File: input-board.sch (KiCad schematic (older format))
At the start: 70 parts, among them J1 BTNCON, J12 CAN, J2 BTNCON, J7 I2C, J8 GAS, J9 BREMSE, SW1 switch-with-led, SW2 switch-with-led, SW3 switch-with-led, SW4 switch-with-led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

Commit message: start of layout
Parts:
- D1, D2, D3, D4, D5, D6, D7, D8: symbol boardcomputer:CDSOD323 -> input-board-rescue:CDSOD323-boardcomputer
- J2: footprint Connector_Molex:Molex_PicoBlade_53047-0410_1x04_P1.25mm_Vertical -> Connector_Molex:Molex_PicoBlade_53048-0410_1x04_P1.25mm_Horizontal
- SW1, SW2, SW3, SW4: footprint input-board:switch-19mm -> input-board:switch-16mm
- U1: symbol boardcomputer:MPM3620 -> input-board-rescue:MPM3620-boardcomputer
- gave numbers to parts that had none: 9
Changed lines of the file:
@@
 	6650 5700 6450 5700
 $Comp
-L boardcomputer:MPM3620 U1
+L input-board-rescue:MPM3620-boardcomputer U1
 U 1 1 601CF94B
 P 8950 1450
@@
 	5300 4950 5300 4850
 $Comp
-L boardcomputer:CDSOD323 D1
+L input-board-rescue:CDSOD323-boardcomputer D1
 U 1 1 60339500
 P 8150 5800
@@
 F 0 "SW4" H 1200 4021 50  0000 C CNN
 F 1 "switch-with-led" H 1200 3930 50  0000 C CNN
-F 2 "input-board:switch-19mm" H 1150 3650 50  0001 C CNN
+F 2 "input-board:switch-16mm" H 1150 3650 50  0001 C CNN
 F 3 "" H 1150 3650 50  0001 C CNN
 	1    1200 3650
@@
 F 0 "SW3" H 1200 3121 50  0000 C CNN
 F 1 "switch-with-led" H 1200 3030 50  0000 C CNN
-F 2 "input-board:switch-19mm" H 1150 2750 50  0001 C CNN
+F 2 "input-board:switch-16mm" H 1150 2750 50  0001 C CNN
 F 3 "" H 1150 2750 50  0001 C CNN
 	1    1200 2750
@@
 F 0 "SW2" H 1200 2271 50  0000 C CNN
 F 1 "switch-with-led" H 1200 2180 50  0000 C CNN
-F 2 "input-board:switch-19mm" H 1150 1900 50  0001 C CNN
+F 2 "input-board:switch-16mm" H 1150 1900 50  0001 C CNN
 F 3 "" H 1150 1900 50  0001 C CNN
 	1    1200 1900
@@
 F 0 "SW1" H 1200 1421 50  0000 C CNN
 F 1 "switch-with-led" H 1200 1330 50  0000 C CNN
-F 2 "input-board:switch-19mm" H 1150 1050 50  0001 C CNN
+F 2 "input-board:switch-16mm" H 1150 1050 50  0001 C CNN
 F 3 "" H 1150 1050 50  0001 C CNN
 	1    1200 1050
@@
 	9250 6000 9550 6000
 $Comp
-L boardcomputer:CDSOD323 D2
+L input-board-rescue:CDSOD323-boardcomputer D2
 U 1 1 603375D7
 P 9850 5800
@@
 	3250 2600 3550 2600
 $Comp
-L boardcomputer:CDSOD323 D4
+L input-board-rescue:CDSOD323-boardcomputer D4
 U 1 1 6033E4AF
 P 3550 2400
@@
 	3250 3300 3550 3300
 $Comp
-L boardcomputer:CDSOD323 D5
-U 1 1 603B76B7
-P 3550 3100
-F 0 "D5" V 3554 3230 50  0000 L CNN
-F 1 "CDSOD323" V 3645 3230 50  0000 L CNN
-F 2 "Diode_SMD:D_SOD-323" H 3550 3250 50  0001 C CNN
-F 3 "" H 3550 3250 50  0001 C CNN
-	1    3550 3100
-	0    1    1    0
-$EndComp
-$Comp
 L Device:C C7
 U 1 1 603B76BD
@@
 	3250 1900 3550 1900
 $Comp
-L boardcomputer:CDSOD323 D3
+L input-board-rescue:CDSOD323-boardcomputer D3
 U 1 1 603C8813
 P 3550 1700
@@
 F 0 "J2" V 2114 4212 50  0000 R CNN
 F 1 "BTNCON" V 2250 4650 50  0000 R CNN
-F 2 "Connector_Molex:Molex_PicoBlade_53047-0410_1x04_P1.25mm_Vertical" H 2150 4500 50  0001 C CNN
+F 2 "Connector_Molex:Molex_PicoBlade_53048-0410_1x04_P1.25mm_Horizontal" H 2150 4500 50  0001 C CNN
 F 3 "~" H 2150 4500 50  0001 C CNN
 	1    2150 4500
@@
 	3250 4700 3550 4700
 $Comp
-L boardcomputer:CDSOD323 D7
+L input-board-rescue:CDSOD323-boardcomputer D7
 U 1 1 60404627
 P 3550 4500
@@
 	3250 5400 3550 5400
 $Comp
-L boardcomputer:CDSOD323 D8
+L input-board-rescue:CDSOD323-boardcomputer D8
 U 1 1 60404651
 P 3550 5200
@@
 	3250 4000 3550 4000
 $Comp
-L boardcomputer:CDSOD323 D6
+L input-board-rescue:CDSOD323-boardcomputer D6
 U 1 1 6040467B
 P 3550 3800
@@
 MDLED4
 $Comp
-L Connector_Generic:Conn_01x04 J?
+L Connector_Generic:Conn_01x04 J3
 U 1 1 604193E6
 P 7100 4750
-F 0 "J?" V 7064 4462 50  0000 R CNN
+F 0 "J3" V 7064 4462 50  0000 R CNN
 F 1 "SWD" V 7200 4900 50  0000 R CNN
 F 2 "Connector_PinHeader_2.54mm:PinHeader_1x04_P2.54mm_Vertical" H 7100 4750 50  0001 C CNN
@@
 SWDIO
 $Comp
-L power:GND #PWR?
+L power:GND #PWR0105
 U 1 1 604368D8
 P 7300 4850
-F 0 "#PWR?" H 7300 4600 50  0001 C CNN
+F 0 "#PWR0105" H 7300 4600 50  0001 C CNN
 F 1 "GND" V 7305 4722 50  0000 R CNN
 F 2 "" H 7300 4850 50  0001 C CNN
@@
 $EndComp
 $Comp
-L power:+3V3 #PWR?
+L power:+3V3 #PWR0106
 U 1 1 60436CB5
 P 7300 4550
-F 0 "#PWR?" H 7300 4400 50  0001 C CNN
+F 0 "#PWR0106" H 7300 4400 50  0001 C CNN
 F 1 "+3V3" H 7315 4723 50  0000 C CNN
 F 2 "" H 7300 4550 50  0001 C CNN
@@
 $EndComp
 $Comp
-L Device:R R?
+L Device:R R24
 U 1 1 604431E6
 P 4750 950
-F 0 "R?" V 4850 950 50  0000 L CNN
+F 0 "R24" V 4850 950 50  0000 L CNN
 F 1 "10k" V 4850 800 50  0000 L CNN
 F 2 "Resistor_SMD:R_0603_1608Metric" V 4680 950 50  0001 C CNN
@@
 $EndComp
 $Comp
-L power:+3V3 #PWR?
+L power:+3V3 #PWR0107
 U 1 1 604431EC
 P 4750 800
-F 0 "#PWR?" H 4750 650 50  0001 C CNN
+F 0 "#PWR0107" H 4750 650 50  0001 C CNN
 F 1 "+3V3" H 4765 973 50  0000 C CNN
 F 2 "" H 4750 800 50  0001 C CNN
@@
 	4750 1100 5000 1100
 $Comp
-L Device:R R?
+L Device:R R25
 U 1 1 6045D388
 P 4750 2400
-F 0 "R?" V 4850 2450 50  0000 L CNN
+F 0 "R25" V 4850 2450 50  0000 L CNN
 F 1 "100k" V 4850 2250 50  0000 L CNN
 F 2 "Resistor_SMD:R_0603_1608Metric" V 4680 2400 50  0001 C CNN
@@
 $EndComp
 $Comp
-L power:GND #PWR?
+L power:GND #PWR0108
 U 1 1 6045DA92
 P 4500 2400
-F 0 "#PWR?" H 4500 2150 50  0001 C CNN
+F 0 "#PWR0108" H 4500 2150 50  0001 C CNN
 F 1 "GND" V 4505 2272 50  0000 R CNN
 F 2 "" H 4500 2400 50  0001 C CNN
@@
 	4600 2400 4500 2400
 $Comp
-L Device:R R?
+L Device:R R23
 U 1 1 6047099B
 P 4500 950
-F 0 "R?" V 4600 950 50  0000 L CNN
+F 0 "R23" V 4600 950 50  0000 L CNN
 F 1 "10k" V 4600 800 50  0000 L CNN
 F 2 "Resistor_SMD:R_0603_1608Metric" V 4430 950 50  0001 C CNN
@@
 $EndComp
 $Comp
-L Device:R R?
+L Device:R R22
 U 1 1 6047A8E0
 P 4300 1300
-F 0 "R?" V 4400 1300 50  0000 L CNN
+F 0 "R22" V 4400 1300 50  0000 L CNN
 F 1 "10k" V 4400 1150 50  0000 L CNN
 F 2 "Resistor_SMD:R_0603_1608Metric" V 4230 1300 50  0001 C CNN
@@
 $EndComp
 $Comp
-L power:GND #PWR?
+L power:GND #PWR0109
 U 1 1 6047AFB7
 P 4100 1350
-F 0 "#PWR?" H 4100 1100 50  0001 C CNN
+F 0 "#PWR0109" H 4100 1100 50  0001 C CNN
 F 1 "GND" V 4105 1222 50  0000 R CNN
 F 2 "" H 4100 1350 50  0001 C CNN
@@
 	4500 1300 5000 1300
 $Comp
-L power:+3V3 #PWR?
+L power:+3V3 #PWR0110
 U 1 1 604A0FE2
 P 4500 800
-F 0 "#PWR?" H 4500 650 50  0001 C CNN
+F 0 "#PWR0110" H 4500 650 50  0001 C CNN
 F 1 "+3V3" H 4515 973 50  0000 C CNN
 F 2 "" H 4500 800 50  0001 C CNN
@@
 RAW_BREMSE
 $Comp
-L Device:C C?
+L Device:C C13
 U 1 1 604A5B63
 P 6550 1450
-F 0 "C?" H 6650 1550 50  0000 C CNN
+F 0 "C13" H 6650 1550 50  0000 C CNN
 F 1 "100n" H 6450 1550 50  0000 C CNN
 F 2 "Capacitor_SMD:C_0603_1608Metric" H 6588 1300 50  0001 C CNN
@@
 $EndComp
 $Comp
-L power:+3V3 #PWR?
+L power:+3V3 #PWR0111
 U 1 1 604A70A4
 P 6550 1300
-F 0 "#PWR?" H 6550 1150 50  0001 C CNN
+F 0 "#PWR0111" H 6550 1150 50  0001 C CNN
 F 1 "+3V3" H 6565 1473 50  0000 C CNN
 F 2 "" H 6550 1300 50  0001 C CNN
@@
 $EndComp
 $Comp
-L power:GND #PWR?
+L power:GND #PWR0112
 U 1 1 604A7536
 P 6550 1600
-F 0 "#PWR?" H 6550 1350 50  0001 C CNN
+F 0 "#PWR0112" H 6550 1350 50  0001 C CNN
 F 1 "GND" V 6555 1472 50  0000 R CNN
 F 2 "" H 6550 1600 50  0001 C CNN
@@
 $EndComp
 $Comp
-L Device:C C?
+L Device:C C14
 U 1 1 604B1696
 P 6900 1450
-F 0 "C?" H 7000 1550 50  0000 C CNN
+F 0 "C14" H 7000 1550 50  0000 C CNN
 F 1 "100n" H 6800 1550 50  0000 C CNN
 F 2 "Capacitor_SMD:C_0603_1608Metric" H 6938 1300 50  0001 C CNN
@@
 $EndComp
 $Comp
-L power:+3V3 #PWR?
+L power:+3V3 #PWR0113
 U 1 1 604B169C
 P 6900 1300
-F 0 "#PWR?" H 6900 1150 50  0001 C CNN
+F 0 "#PWR0113" H 6900 1150 50  0001 C CNN
 F 1 "+3V3" H 6915 1473 50  0000 C CNN
 F 2 "" H 6900 1300 50  0001 C CNN
@@
 $EndComp
 $Comp
-L power:GND #PWR?
+L power:GND #PWR0114
 U 1 1 604B16A2
 P 6900 1600
-F 0 "#PWR?" H 6900 1350 50  0001 C CNN
+F 0 "#PWR0114" H 6900 1350 50  0001 C CNN
 F 1 "GND" V 6905 1472 50  0000 R CNN
 F 2 "" H 6900 1600 50  0001 C CNN
@@
 $EndComp
 $Comp
-L Device:C C?
+L Device:C C15
 U 1 1 604BAED3
 P 7250 1450
-F 0 "C?" H 7350 1550 50  0000 C CNN
+F 0 "C15" H 7350 1550 50  0000 C CNN
 F 1 "100n" H 7150 1550 50  0000 C CNN
 F 2 "Capacitor_SMD:C_0603_1608Metric" H 7288 1300 50  0001 C CNN
@@
 $EndComp
 $Comp
-L power:+3V3 #PWR?
+L power:+3V3 #PWR0115
 U 1 1 604BAED9
 P 7250 1300
-F 0 "#PWR?" H 7250 1150 50  0001 C CNN
+F 0 "#PWR0115" H 7250 1150 50  0001 C CNN
 F 1 "+3V3" H 7265 1473 50  0000 C CNN
 F 2 "" H 7250 1300 50  0001 C CNN
@@
 $EndComp
 $Comp
-L power:GND #PWR?
+L power:GND #PWR0116
 U 1 1 604BAEDF
 P 7250 1600
-F 0 "#PWR?" H 7250 1350 50  0001 C CNN
+F 0 "#PWR0116" H 7250 1350 50  0001 C CNN
 F 1 "GND" V 7255 1472 50  0000 R CNN
 F 2 "" H 7250 1600 50  0001 C CNN
@@
 $EndComp
 $Comp
-L Device:C C?
+L Device:C C16
 U 1 1 604C50A6
 P 7250 2300
-F 0 "C?" H 7350 2400 50  0000 C CNN
+F 0 "C16" H 7350 2400 50  0000 C CNN
 F 1 "100n" H 7150 2400 50  0000 C CNN
 F 2 "Capacitor_SMD:C_0603_1608Metric" H 7288 2150 50  0001 C CNN
@@
 $EndComp
 $Comp
-L power:+3V3 #PWR?
+L power:+3V3 #PWR0117
 U 1 1 604C50AC
 P 7250 2150
-F 0 "#PWR?" H 7250 2000 50  0001 C CNN
+F 0 "#PWR0117" H 7250 2000 50  0001 C CNN
 F 1 "+3V3" H 7265 2323 50  0000 C CNN
 F 2 "" H 7250 2150 50  0001 C CNN
@@
 $EndComp
 $Comp
-L power:GND #PWR?
+L power:GND #PWR0122
 U 1 1 604C50B2
 P 7250 2450
-F 0 "#PWR?" H 7250 2200 50  0001 C CNN
+F 0 "#PWR0122" H 7250 2200 50  0001 C CNN
 F 1 "GND" V 7255 2322 50  0000 R CNN
 F 2 "" H 7250 2450 50  0001 C CNN
@@
 	1    0    0    -1
 $EndComp
+$Comp
+L input-board-rescue:CDSOD323-boardcomputer D5
+U 1 1 603B76B7
+P 3550 3100
+F 0 "D5" V 3554 3230 50  0000 L CNN
+F 1 "CDSOD323" V 3645 3230 50  0000 L CNN
+F 2 "Diode_SMD:D_SOD-323" H 3550 3250 50  0001 C CNN
+F 3 "" H 3550 3250 50  0001 C CNN
+	1    3550 3100
+	0    1    1    0
+$EndComp
 $EndSCHEMATC

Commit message: more layouting
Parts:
- added C17: 100n, Capacitor_SMD:C_0603_1608Metric, symbol Device:C
- added X1: ASCO, Oscillator:Oscillator_SMD_Abracon_ASDMB-4Pin_2.5x2.0mm, symbol Oscillator:ASDMB-xxxMHz
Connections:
- net +3V3: now also C17.2, X1.1 (Standby), X1.4 (VDD)
- net BTN1: now also U2.40 (PB4); no longer U2.39 (PB3)
- net BTN2: now also U2.39 (PB3); no longer U2.40 (PB4)
- net BTN3: now also U2.38 (PA15); no longer U2.31 (PA10)
- net BTN4: now also U2.25 (PB12); no longer U2.42 (PB6)
- net BTN5: now also U2.22 (PB11); no longer U2.43 (PB7)
- net BTN6: now also U2.21 (PB10); no longer U2.38 (PA15)
- net GND: now also SW1.2, SW2.2, C17.1, X1.2 (GND); no longer SW1.1, SW2.1
- net MDBT1: now also SW1.1, U2.43 (PB7); no longer SW1.2, U2.18 (PB0)
- net MDBT2: now also SW2.1, U2.29 (PA8); no longer SW2.2, U2.21 (PB10)
- net MDBT3: now also U2.26 (PB13); no longer U2.25 (PB12)
- net MDBT4: now also U2.18 (PB0); no longer U2.27 (PB14)
- net MDLED1: now also U2.42 (PB6); no longer U2.19 (PB1)
- net MDLED2: now also U2.28 (PB15); no longer U2.22 (PB11)
- net MDLED3: now also U2.27 (PB14); no longer U2.26 (PB13)
- net MDLED4: now also U2.19 (PB1); no longer U2.28 (PB15)
- net at U2.5 (PD0): now also X1.3 (Out)
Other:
- note added: "3V3"
- note added: "5V"
- moved on the sheet: C5, C6, C7, D3, D4, D5, J1, R11, R17, R18, R5, R6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

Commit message: Added input reverse protection
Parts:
- added D9: D_Schottky, Diode_SMD:D_SOD-123, symbol Device:D_Schottky
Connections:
- net 15V: now also D9.1 (K); no longer J12.1 (Pin_1)
- new net: D9.2 (A), J12.1 (Pin_1)
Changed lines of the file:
@@
 Text GLabel 6650 5400 2    50   Input ~ 0
 GND
-Text GLabel 6650 5700 2    50   Input ~ 0
+Text GLabel 6750 5700 2    50   Input ~ 0
 15V
 Text GLabel 6650 5600 2    50   Input ~ 0
@@
 Wire Wire Line
 	6450 5600 6650 5600
-Wire Wire Line
-	6650 5700 6450 5700
 $Comp
 L input-board-rescue:MPM3620-boardcomputer U1
@@
 3V3
 $Comp
-L power:GND #PWR?
+L power:GND #PWR027
 U 1 1 6045ABEF
 P 1400 4200
-F 0 "#PWR?" H 1400 3950 50  0001 C CNN
+F 0 "#PWR027" H 1400 3950 50  0001 C CNN
 F 1 "GND" V 1405 4027 50  0000 C CNN
 F 2 "" H 1400 4200 50  0001 C CNN
@@
 $EndComp
 $Comp
-L power:GND #PWR?
+L power:GND #PWR028
 U 1 1 6045B33D
 P 1400 5050
-F 0 "#PWR?" H 1400 4800 50  0001 C CNN
+F 0 "#PWR028" H 1400 4800 50  0001 C CNN
 F 1 "GND" V 1405 4877 50  0000 C CNN
 F 2 "" H 1400 5050 50  0001 C CNN
@@
 	0    -1   -1   0
 $EndComp
+$Comp
+L Device:D_Schottky D9
+U 1 1 603427AF
+P 6600 5700
+F 0 "D9" H 6750 5800 50  0000 C CNN
+F 1 "D_Schottky" H 6450 5800 50  0000 C CNN
+F 2 "Diode_SMD:D_SOD-123" H 6600 5700 50  0001 C CNN
+F 3 "~" H 6600 5700 50  0001 C CNN
+	1    6600 5700
+	-1   0    0    1
+$EndComp
 $EndSCHEMATC

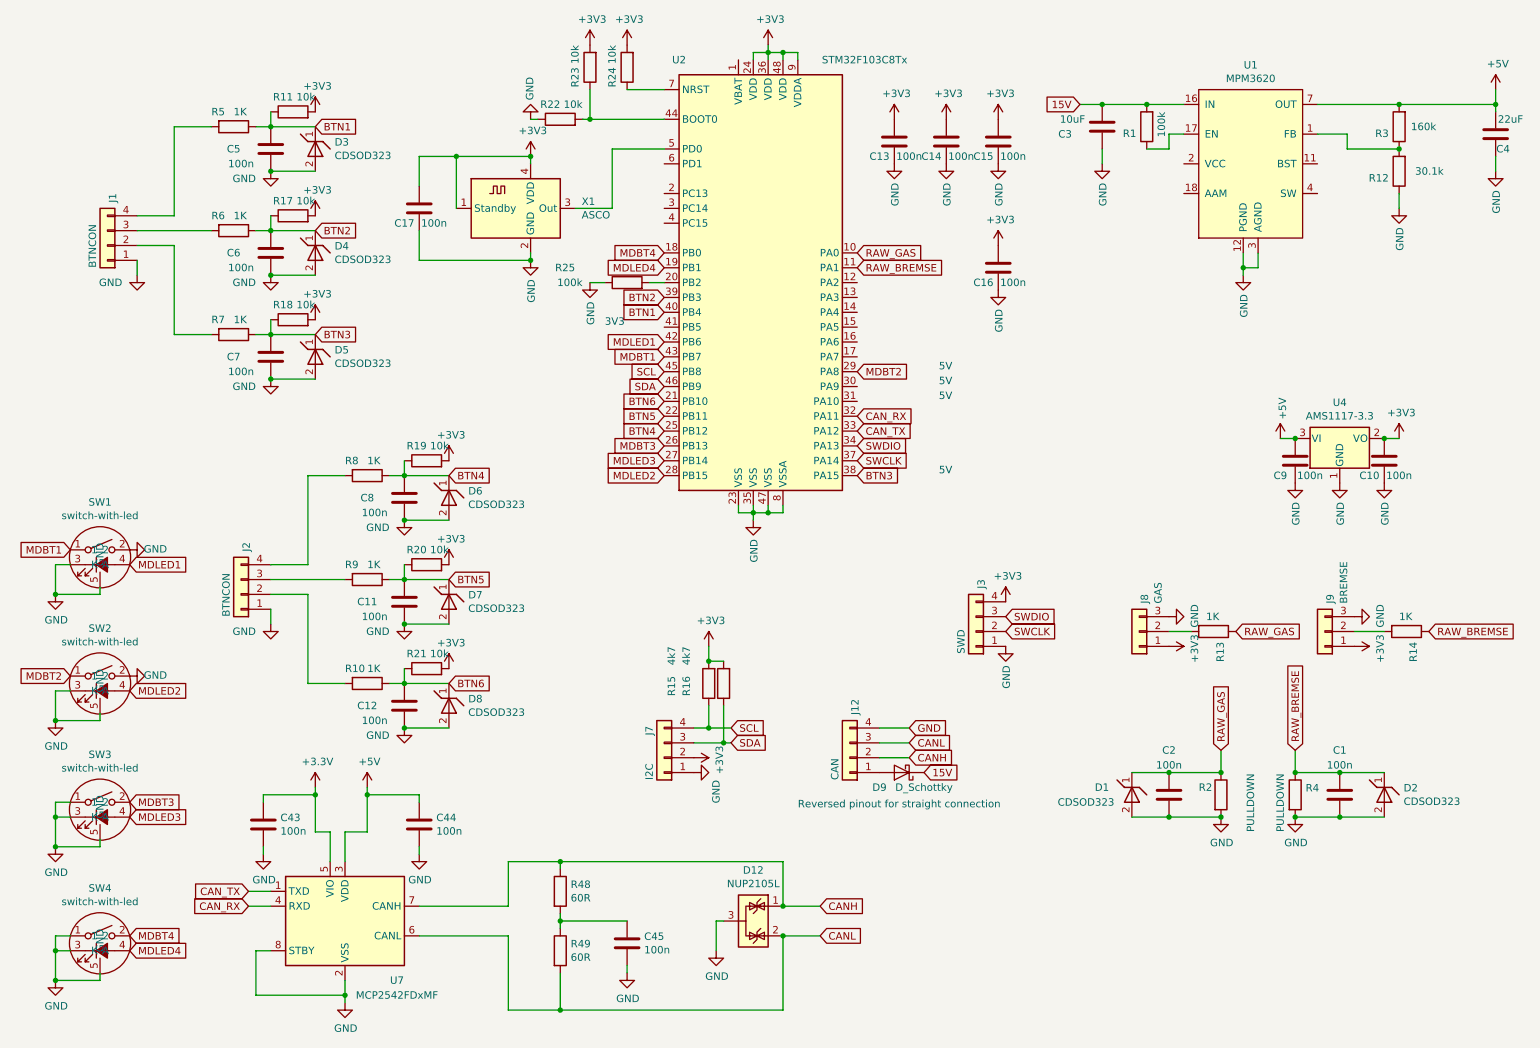
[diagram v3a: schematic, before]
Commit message: Changed input to LDO Added JLCPCB #
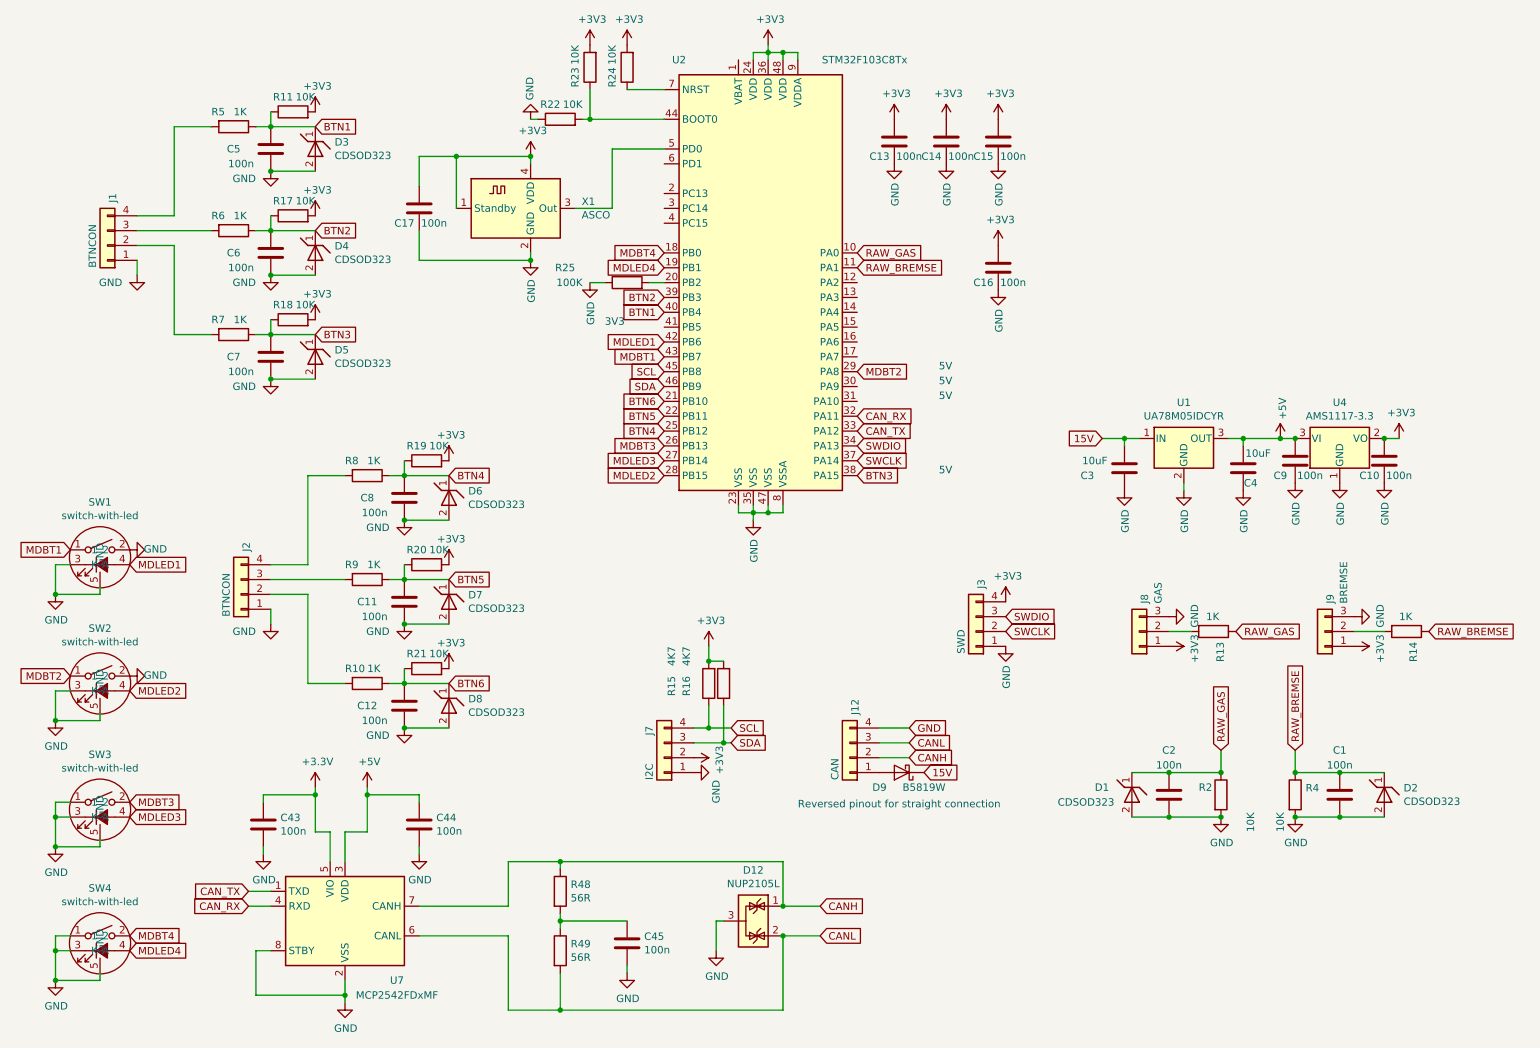
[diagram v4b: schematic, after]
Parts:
- removed R1: 100k, Resistor_SMD:R_0603_1608Metric, symbol Device:R
- removed R12: 30.1k, Resistor_SMD:R_0603_1608Metric, symbol Device:R
- removed R3: 160k, Resistor_SMD:R_0603_1608Metric, symbol Device:R
- removed U1: MPM3620, boardcomputer:QFN-20-1EP_3x5mm_P0.85mm, symbol input-board-rescue:MPM3620-boardcomputer
- added U1: UA78M05IDCYR, Package_TO_SOT_SMD:SOT-223-3_TabPin2, symbol Regulator_Linear:uA7805
- C1, C10, C11, C12, C13, C14, C15, C16, C17, C2, C43, C44, C45, C5, C6, C7, C8, C9: LCSC Part # (none) -> C14663
- C3: LCSC Part # (none) -> C15850
- C4: value 22uF -> 10uF; LCSC Part # (none) -> C15850
- D1, D2, D3, D4, D5, D6, D7, D8: LCSC Part # (none) -> C127526
- D12: LCSC Part # (none) -> C284104
- D9: value D_Schottky -> B5819W; LCSC Part # (none) -> C8598
- J1: footprint Connector_Molex:Molex_PicoBlade_53047-0410_1x04_P1.25mm_Vertical -> Connector_Molex:Molex_PicoBlade_53048-0410_1x04_P1.25mm_Horizontal
- R10, R13, R14, R5, R6, R7, R8, R9: LCSC Part # (none) -> C21190
- R11, R17, R18, R19, R20, R21, R22, R23, R24: value 10k -> 10K; LCSC Part # (none) -> C25804
- R15, R16: value 4k7 -> 4K7; LCSC Part # (none) -> C23162
- R2, R4: value PULLDOWN -> 10K; LCSC Part # (none) -> C25804
- R25: value 100k -> 100K; LCSC Part # (none) -> C25803
- R48, R49: value 60R -> 56R; LCSC Part # (none) -> C25196
- U2: LCSC Part # (none) -> C8304
- U4: LCSC Part # (none) -> C6186
- X1: LCSC Part # (none) -> C387448
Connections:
- net +5V: now also U1.3 (OUT)
- net 15V: now also U1.1 (IN)
- net GND: now also U1.2 (GND)
